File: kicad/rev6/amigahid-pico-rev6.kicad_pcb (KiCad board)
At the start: 2 copper layers, 100 x 80 mm, 115 parts, among them J1 A500 KBD OUT, J10 PS/2 KBD OUT, J11 DIN5 KBD IN, J12 PS/2 KBD IN, J13 USB-C AUX 5V, J2 DEBUG UART+SWD, J3 OLED I2C, J4 USB-A HOST, J7 SPARE GP28, J8 A500 KBD IN, J9 DIN5 KBD OUT, P1 DE9 MALE PORT 1, P2 DE9 MALE PORT 2, Q1 BSS138, Q10 BSS138, Q11 BSS138, Q12 BSS138, Q13 BSS138, Q14 BSS138, Q15 BSS138, Q16 BSS138, Q17 BSS138, Q18 BSS138, Q19 BSS138, Q2 BSS138, Q3 BSS138, Q4 BSS138, Q5 BSS138, Q6 BSS138, Q7 BSS138, Q8 BSS138, Q9 BSS138, U1 PicoW, U2 USBLC6-2SC6

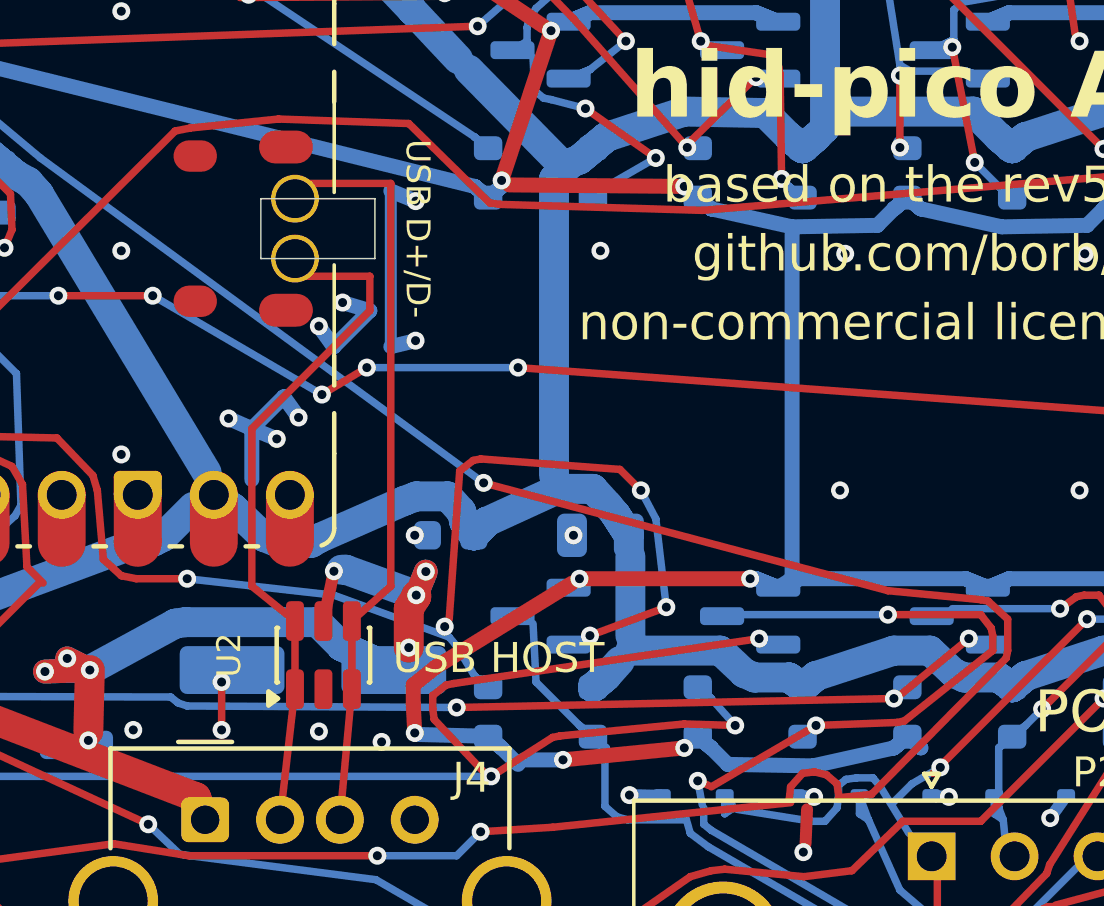
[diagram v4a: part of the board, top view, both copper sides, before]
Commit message: kicad: keep the bottom side flat — move the usb bulk cap topside
all three gates stay green: DRC 0 violations / 0 unconnected, check_rev6_pcb 33/33,
check_rev6_netlist 356/356.

C4, the 150uF USB-host bulk can, was the only thing on the bottom taller than about a
millimetre - a 6.3 x 7.7 mm CP_Elec against a field of 0603s, 0805s, SOT-23s and
SOD-323s - so the board could not sit flat on that face.  it moves to the top at
57.400,64.400 at rot 0, pad 1 (+, USBA_5V) west at 54.700,64.400 and pad 2 (-, GND)
east at 60.100,64.400.

that puts it 10.29 mm from J4 pin 1, against 8.04 mm on the bottom.  it is the closest
legal top-side spot: the courtyard is 9.49 x 7.19 mm and the only band that will take it
is east of the Pico, where the core has to clear U1's east edge at x 51.245 and the
USB-A body at y 68.235; everything further west is under U2 or U1.  the local
high-frequency decoupling does not move - C5 stays 4.7 mm from the VBUS pin on the
bottom - so what lengthens is the bulk path alone, about 2 mm of 1 mm-wide copper.

F2 and U2 are not touched.  the two cap lands do sit across the board's busiest corridor
though, so four nets are re-laid round them:

  +3V3         the diagonal that used to cross the corridor now runs beneath the can and
               climbs the 1.9 mm gap between its two pads.
  cont2_hq_lo  both ends.  the west layer change moves from 54.800,64.550, now under
               pad 1, out to 56.400,62.950, and the trunk north is kneed at 55.100,61.000
               to keep 0.5 mm off cont1_v's via.  the east hop over the SYS5V B.Cu trunk
               moves south of pad 2 and lands at 58.700,65.860, stubbing across to Q16
               pad 2 rather than dropping a via onto it - pad 2 now covers Q16, and no
               via can reach that pad with 0.5 mm of hole clearance any more.
  cont2_vq_lo  kneed at 56.300 and 62.400 to clear pad 2 and leave the hop its lane.
  usb_dp       its corner is pulled back 0.2 mm to 53.000,63.000, clear of pa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
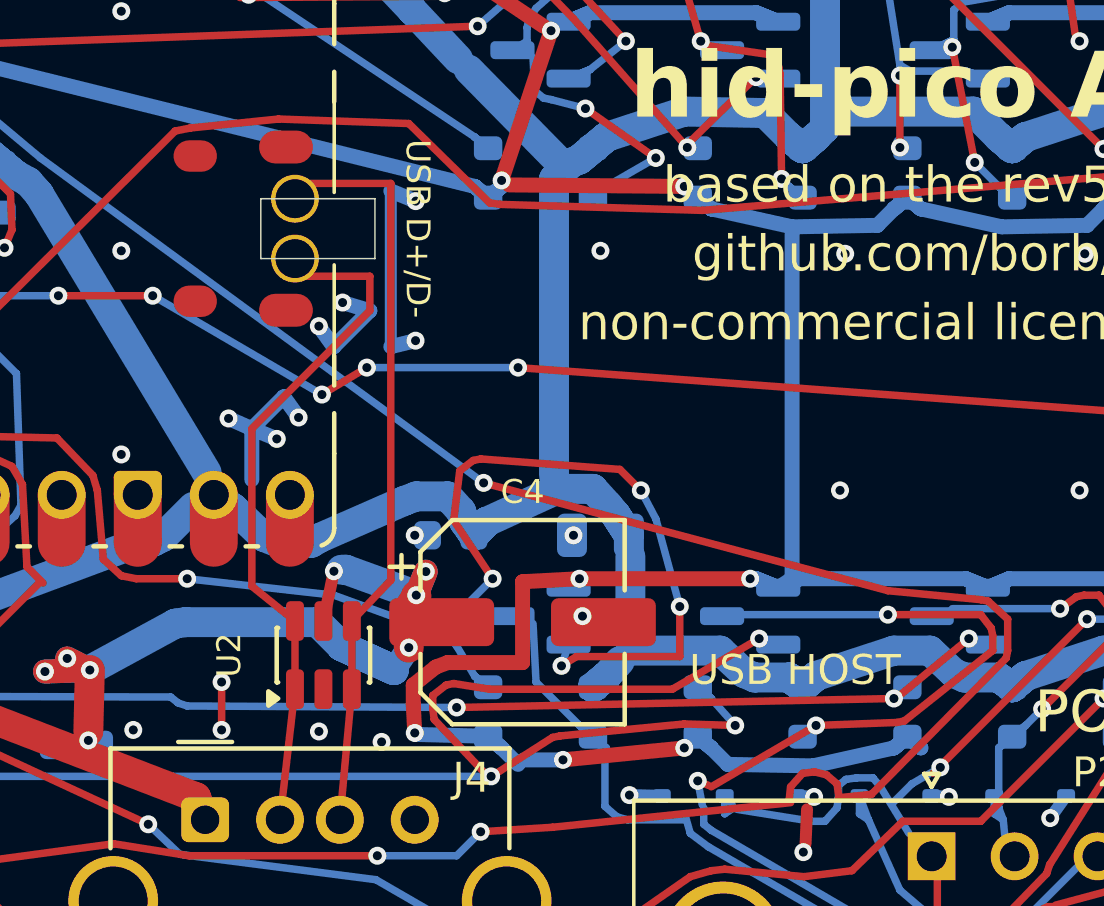
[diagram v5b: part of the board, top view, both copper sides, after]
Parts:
- C4: moved to F.Cu
- moved C4 7.18 mm to (57.4, 64.4), turned to 0 degrees
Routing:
- net /cont2_hq_lo: track 65.2 -> 70.3 mm
- net +3V3: track 433.7 -> 435.9 mm
- net /USBA_5V: track 43.9 -> 44.8 mm
- net GND: vias 121 -> 122

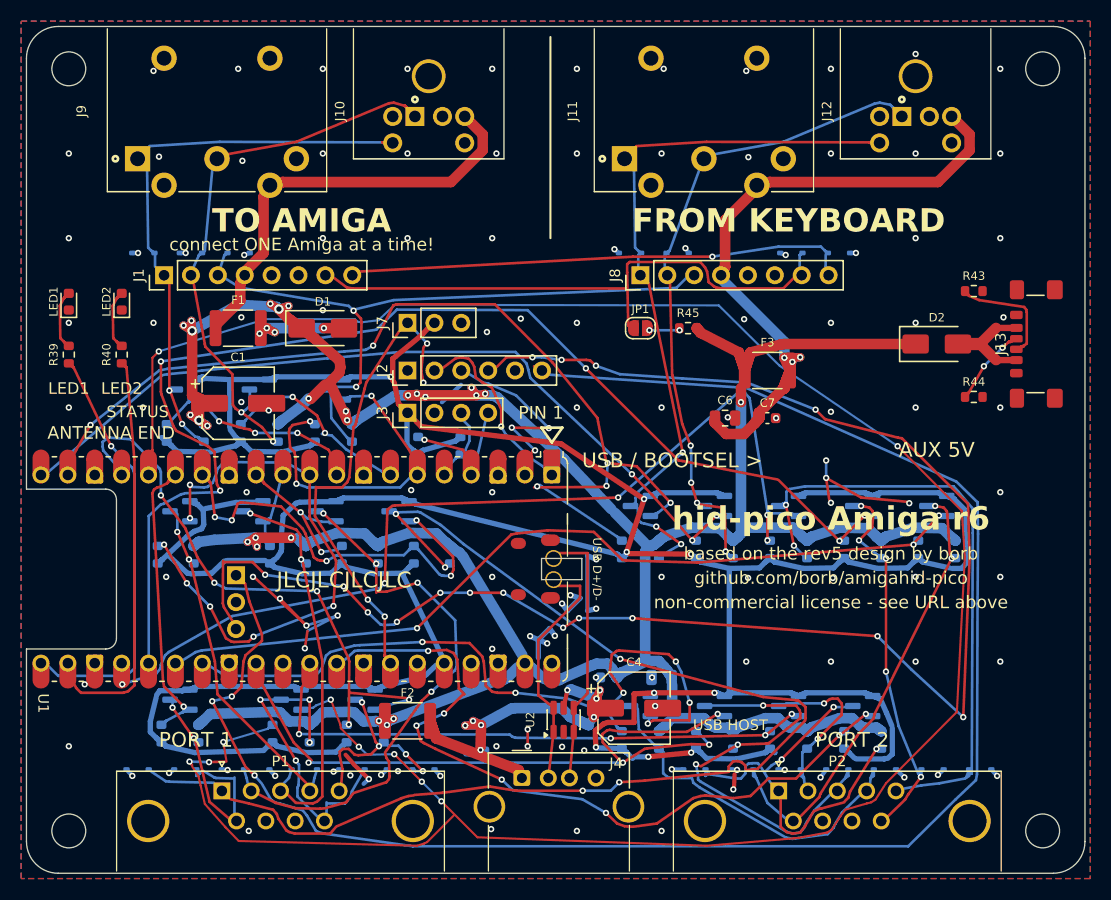
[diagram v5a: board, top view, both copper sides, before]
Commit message: kicad: re-lay the ground ties on 45-degree runs
GND is a poured net: its tracks are the short links between a pad and the
stitching via that takes it to the plane on the other side.  Forty-two of the
fifty-three segments sat at whatever angle the maze router left them at, which
is 54 mm of copper wandering across the board at 5 to 20 degrees off.

Each chain is now torn out and laid again between the same two anchors, as one
straight run or an orthogonal and a 45.  Where the two anchors are a few
hundredths off an exact 45, the tie lands a hair off the pad centre rather
than growing a 50 micron leg to make up the difference - a tenth of a
millimetre inside an 0.8 mm pad is still dead on it.  Forty-four of the
forty-six chains came out clean; the one that did not is a 0.05 mm nub that is
already horizontal.  The stitching vias have not moved.

45 degree compliance 34.4% -> 35.8%, no new debris, no new duplicate copper.
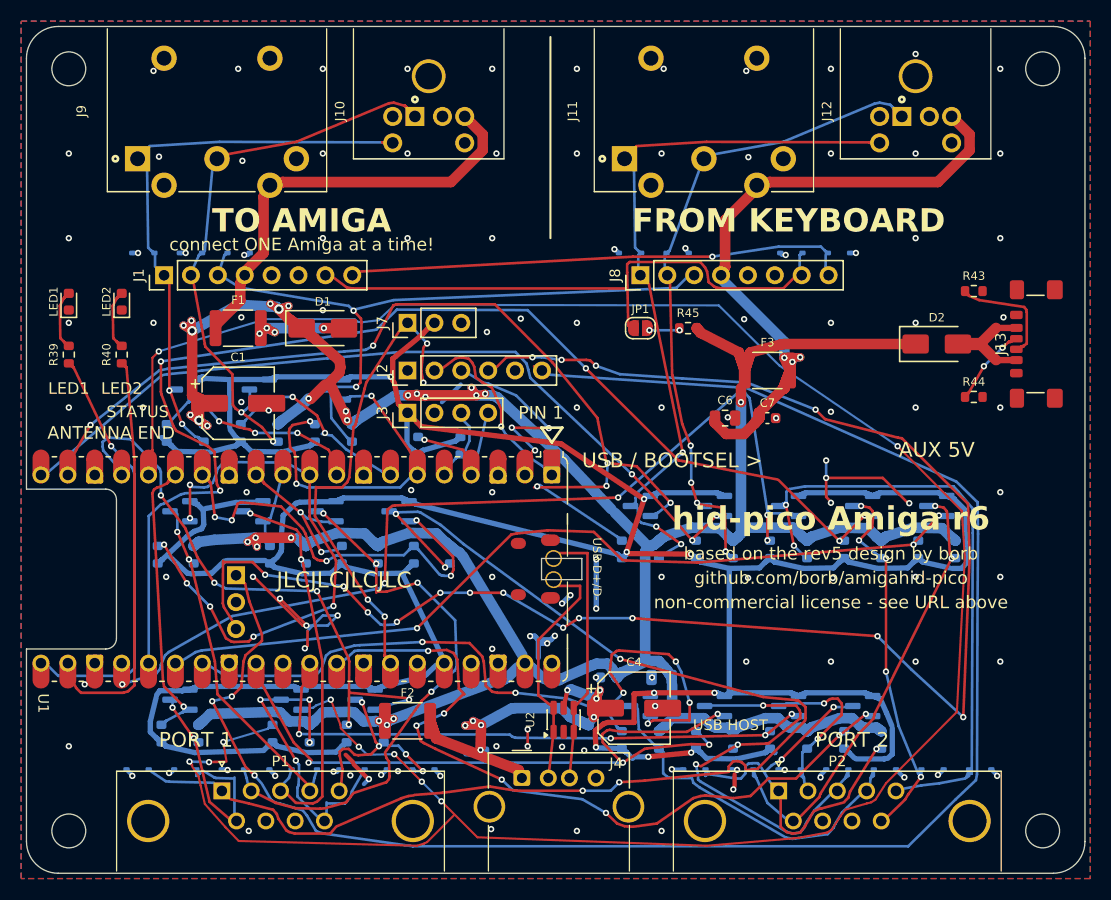
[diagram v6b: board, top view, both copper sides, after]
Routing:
- net GND: track 71.7 -> 67.1 mm

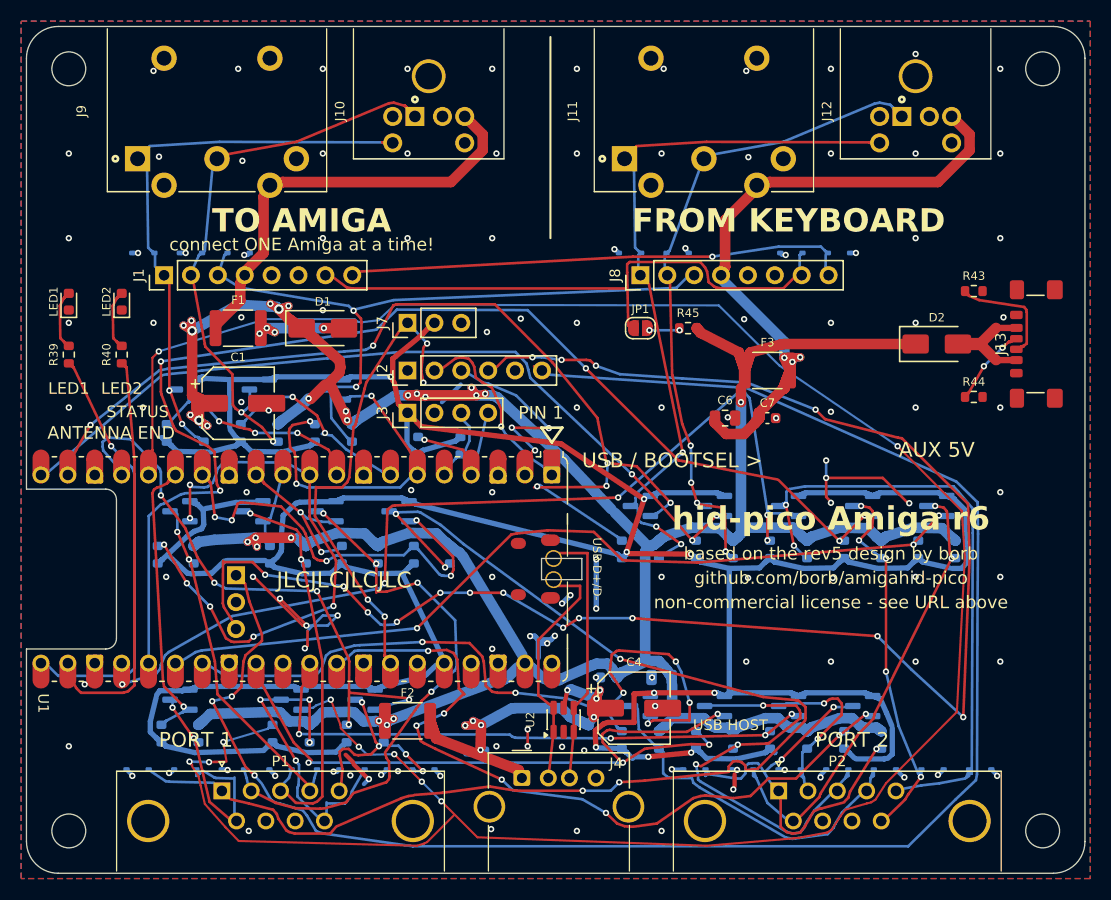
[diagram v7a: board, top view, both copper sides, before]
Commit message: kicad: void the module test-pad copper and tidy the rev6 board
the flat-mount build rests the pico w's bare underside test pads on the
carrier with nothing but solder resist between them, and rev6 was running
live copper under three of them: /cont1_v crossed tp6 (bootsel / qspi_ss),
/cont1_v_lo and /cont1_v crossed tp5, and ground pour filled tp4. tp6 held
low is an rp2040 that boots to mass storage for ever, and /cont1_v is a
5 v-side node pulled to sys5v, so that pad could also see overvoltage on a
3v3 pin. doc/errata.md already records the same class of fault on rev4.

so: both crossings move out, and an f.cu rule area at x 35.40-42.50,
y 47.76-49.76 keeps tracks, vias and pour out for good. /cont1_v_lo now
takes the 1.0 mm channel west of the band - q7 pad 2 straight down to the
existing b.cu node by r13 - which also drops 9 mm of copper and two vias
off that net. /cont1_v goes round the east side. the band covers tp4/tp5/
tp6 of a pico w or pico 2 w and tp5/tp6 of a plain pico; a plain pico's
tp4 is the one position with no room left, and errata says so.

also in this pass:

- 413 exactly duplicated track objects removed, plus four collinear
  slivers hiding inside longer segments of their own net (the 0.1 mm
  reverse stubs on /cont2_b1 and /cont2_b2 and a 0.071 mm +3v3 nub).
  style gate s3 goes green; s1 and s2 stay red, see below.
- the thirteen hand-soldered connectors and u1 get exclude_from_pos_files,
  so a regenerated cpl no longer offers jlc thirteen connectors and a
  51 mm module to place. jp1 already had it.
- u1's four usb shell pads lose their paste apertures. the footprint descr
  has claimed since it was written that reflow paste was deleted; the 40
  castellated pads were, these four were missed, and they sit directly
  under where the module has to lie flat.
- sixteen silkscreen strokes at 0.12 mm go to 0.15 mm, jlc's floor, and
  are pulled 0.02-0.03 mm off the board edge so widening them does not
  break the silk-to-edge rule. the u1 tap sl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
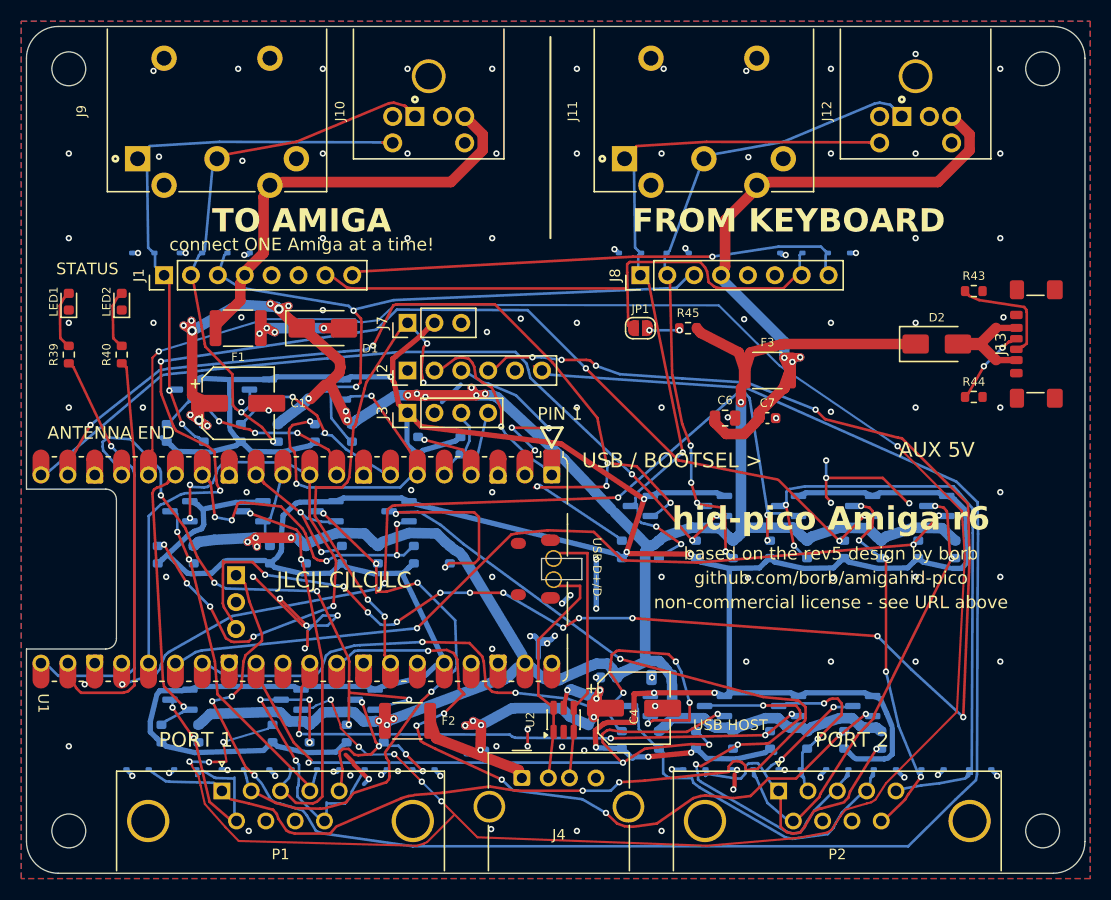
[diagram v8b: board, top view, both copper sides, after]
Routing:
- net +3V3: track 435.9 -> 352.8 mm
- net /SYS5V: track 353.2 -> 293.0 mm
- net /KBIN_5V: track 81.2 -> 65.1 mm
- net /gp28: track 59.4 -> 45.2 mm
- net /cont1_v_lo: track 44.0 -> 34.3 mm
- net /kbclock: track 61.8 -> 53.1 mm
- net /kbdata: track 57.6 -> 49.6 mm
- net /USBA_5V: track 44.8 -> 37.5 mm
- net /cont1_v: track 120.1 -> 127.3 mm
- net /cont1_b2_lo: track 236.2 -> 229.3 mm
- net /AMIGA_5V: track 47.5 -> 40.7 mm
- net /kbdata_lo: track 25.1 -> 18.4 mm
- net /kbin_clk: track 72.3 -> 66.9 mm
- net /usb_cc2: track 13.1 -> 8.27 mm
- net /usb_cc1: track 16.1 -> 11.3 mm
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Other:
- board text removed: "LED1"
- board text removed: "LED2"
